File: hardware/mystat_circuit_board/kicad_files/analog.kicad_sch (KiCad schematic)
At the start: 46 parts, among them J3 SJ1-42534-SMT, K1 9011-05-11, K2 9011-05-11, K3 9011-05-11, K4 9011-05-11, K5 9011-05-11, U10 OPA192, U11 BUF634A, U12 ADG1419, U13 OPA192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

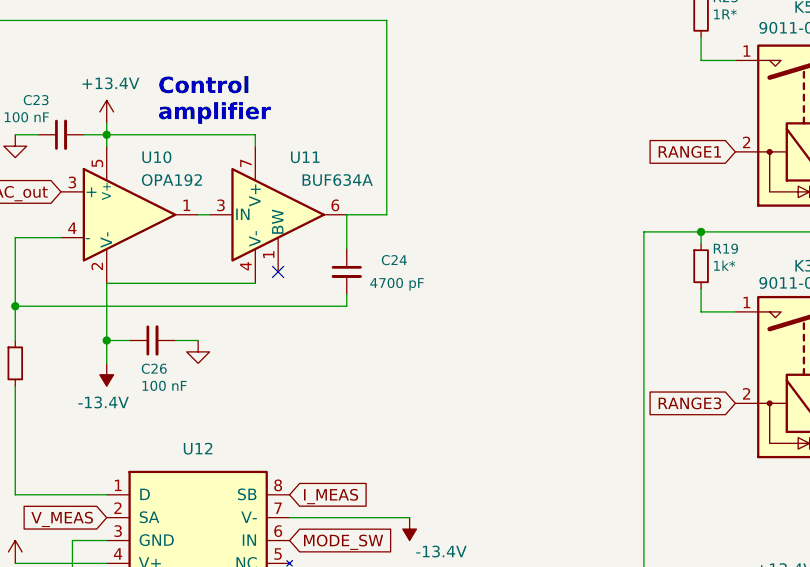
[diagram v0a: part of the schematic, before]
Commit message: merged Daniel's changes in to GUI. getting things ready in KiCAD 10 and finding substitute parts
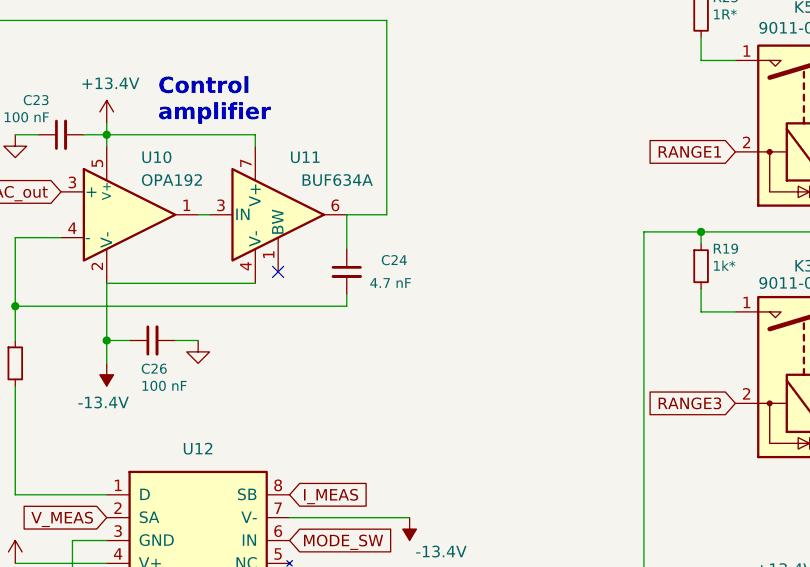
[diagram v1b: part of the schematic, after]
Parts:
- C24: value 4700 pF -> 4.7 nF
- J3: value SJ1-42534-SMT -> SJ1-42534-SMT-TR
- R10: LCSC (none) -> C17594; Manufacturer Panasonic Electronic Components -> UNI-ROYAL; Part Number ERJ-6ENF27R0V -> 0805W8F270JT5E
- R11: LCSC (none) -> C17414; Manufacturer Yageo -> UNI-ROYAL; Part Number RC0805FR-0710KL -> 0805W8F1002T5E
- R12, R14: LCSC (none) -> C2989478; Manufacturer Panasonic Electronic Components -> UNI-ROYAL; Part Number ERA-6AEB4023V -> TC0525B4023T5G
- R13, R15, R17, R18, R20, R22: LCSC (none) -> C136919; Manufacturer Panasonic Electronic Components -> YAGEO; Part Number ERA-6AEB753V -> RT0805BRD0775KL
- R16: LCSC (none) -> C122537; Manufacturer Panasonic Electronic Components -> YAGEO; Part Number ERA-6AEB104V -> RT0805BRD07100KL
- R19: LCSC (none) -> C110774; Manufacturer Panasonic Electronic Components -> YAGEO; Part Number ERA-6AEB102V -> RT0805BRD071KL
- R21: LCSC (none) -> C2988901; Manufacturer Panasonic Electronic Components -> UNI-ROYAL; Part Number ERA-6AEB183V -> TC0525B1802T5G
- R23: LCSC (none) -> C417117; Part Number ERA-6AEB202V -> ERA6AEB202V
- R24: LCSC (none) -> C4209318; Manufacturer TE Connectivity Passive Product -> TE Connectivity; Part Number 2-1625868-7 -> RP73PF2A10RBTDF
- R25: LCSC (none) -> C865286; Manufacturer Susumu -> YAGEO; Part Number RL1220S-1R0-F -> RT0805BRD071RL
- U11: LCSC (none) -> C2058426
- U12: LCSC (none) -> C22368

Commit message: revert to KiCAD 10 state before attempting reed relay changes, to merge into master
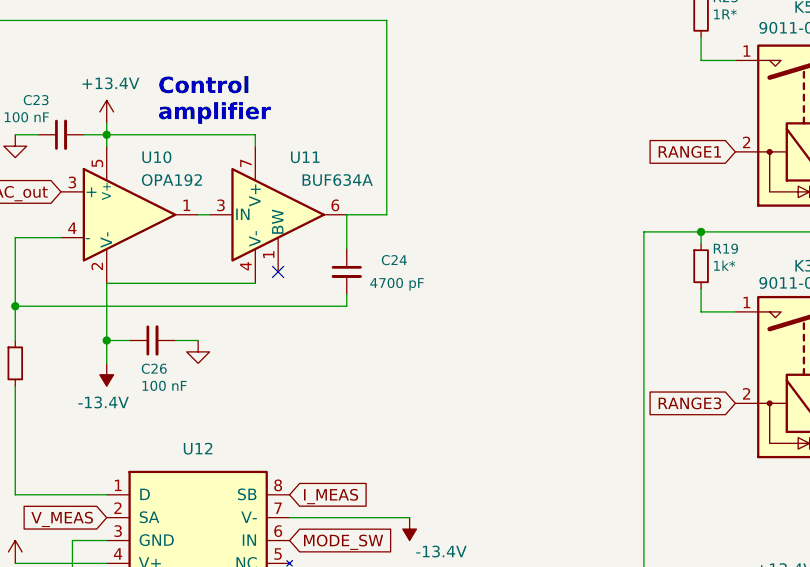
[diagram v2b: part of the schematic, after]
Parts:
- C24: value 4.7 nF -> 4700 pF
- J3: value SJ1-42534-SMT-TR -> SJ1-42534-SMT
- R10: LCSC C17594 -> (none); Manufacturer UNI-ROYAL -> Panasonic Electronic Components; Part Number 0805W8F270JT5E -> ERJ-6ENF27R0V
- R11: LCSC C17414 -> (none); Manufacturer UNI-ROYAL -> Yageo; Part Number 0805W8F1002T5E -> RC0805FR-0710KL
- R12, R14: LCSC C2989478 -> (none); Manufacturer UNI-ROYAL -> Panasonic Electronic Components; Part Number TC0525B4023T5G -> ERA-6AEB4023V
- R13, R15, R17, R18, R20, R22: LCSC C136919 -> (none); Manufacturer YAGEO -> Panasonic Electronic Components; Part Number RT0805BRD0775KL -> ERA-6AEB753V
- R16: LCSC C122537 -> (none); Manufacturer YAGEO -> Panasonic Electronic Components; Part Number RT0805BRD07100KL -> ERA-6AEB104V
- R19: LCSC C110774 -> (none); Manufacturer YAGEO -> Panasonic Electronic Components; Part Number RT0805BRD071KL -> ERA-6AEB102V
- R21: LCSC C2988901 -> (none); Manufacturer UNI-ROYAL -> Panasonic Electronic Components; Part Number TC0525B1802T5G -> ERA-6AEB183V
- R23: LCSC C417117 -> (none); Part Number ERA6AEB202V -> ERA-6AEB202V
- R24: LCSC C4209318 -> (none); Manufacturer TE Connectivity -> TE Connectivity Passive Product; Part Number RP73PF2A10RBTDF -> 2-1625868-7
- R25: LCSC C865286 -> (none); Manufacturer YAGEO -> Susumu; Part Number RT0805BRD071RL -> RL1220S-1R0-F
- U11: LCSC C2058426 -> (none)
- U12: LCSC C22368 -> (none)
